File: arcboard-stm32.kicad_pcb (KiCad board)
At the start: 2 copper layers, 59.5 x 59.7 mm, 78 parts, among them J10 Conn_01x02_Socket, J5 Conn_01x02_Socket, J9 Conn_01x03_Socket, U1 XC6210B332MR-G, U10 1N4148W_C81598, U11 TS-1187A-B-A-B, U12 AO3401A, U13 AO3401A, U14 TS-1187A-B-A-B, U15 TS-1187A-B-A-B, U2 TYPE-C-31-M-13, U3 STM32F405RGTx, U4 PJ-320A, U5 BAV70S,115, U6 BAV70S,115, U7 BAV70S,115, U8 BAV70S,115, U9 BAV70S,115, Y1 Crystal_GND24

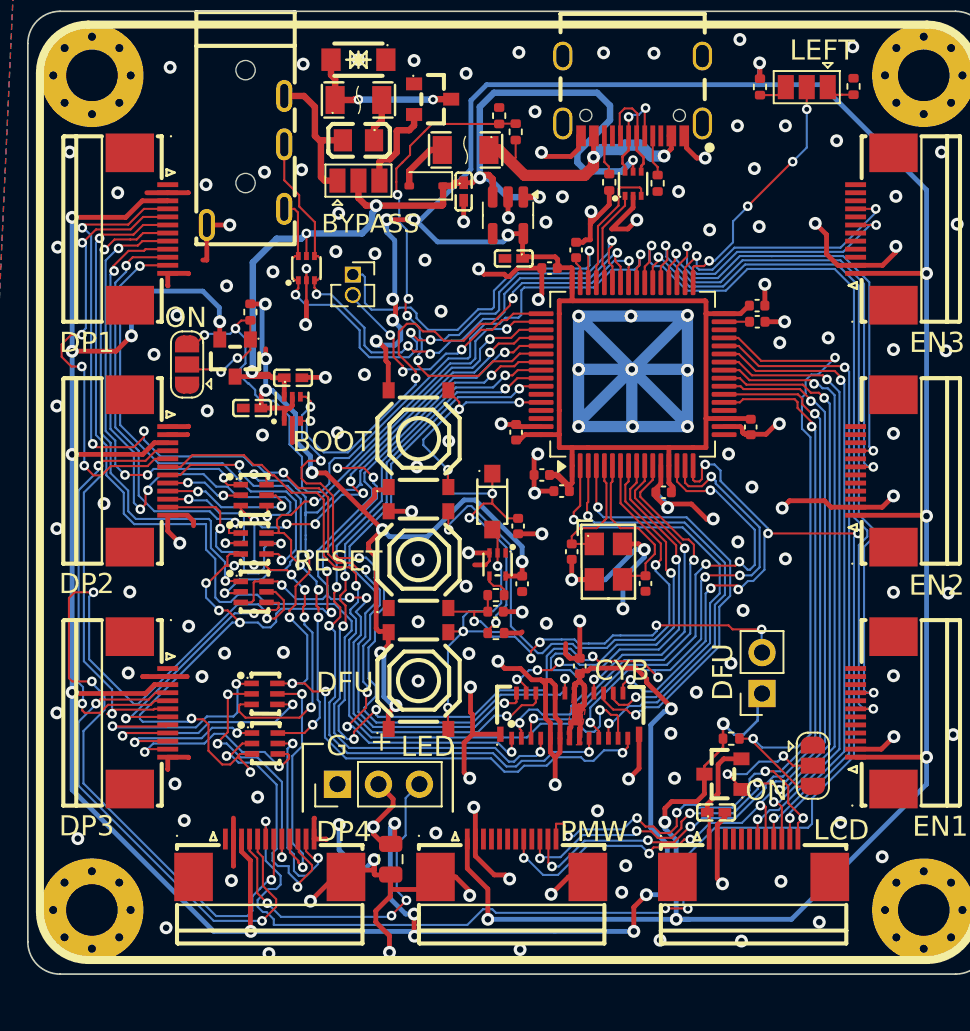
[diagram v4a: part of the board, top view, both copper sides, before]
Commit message: more trace pruning
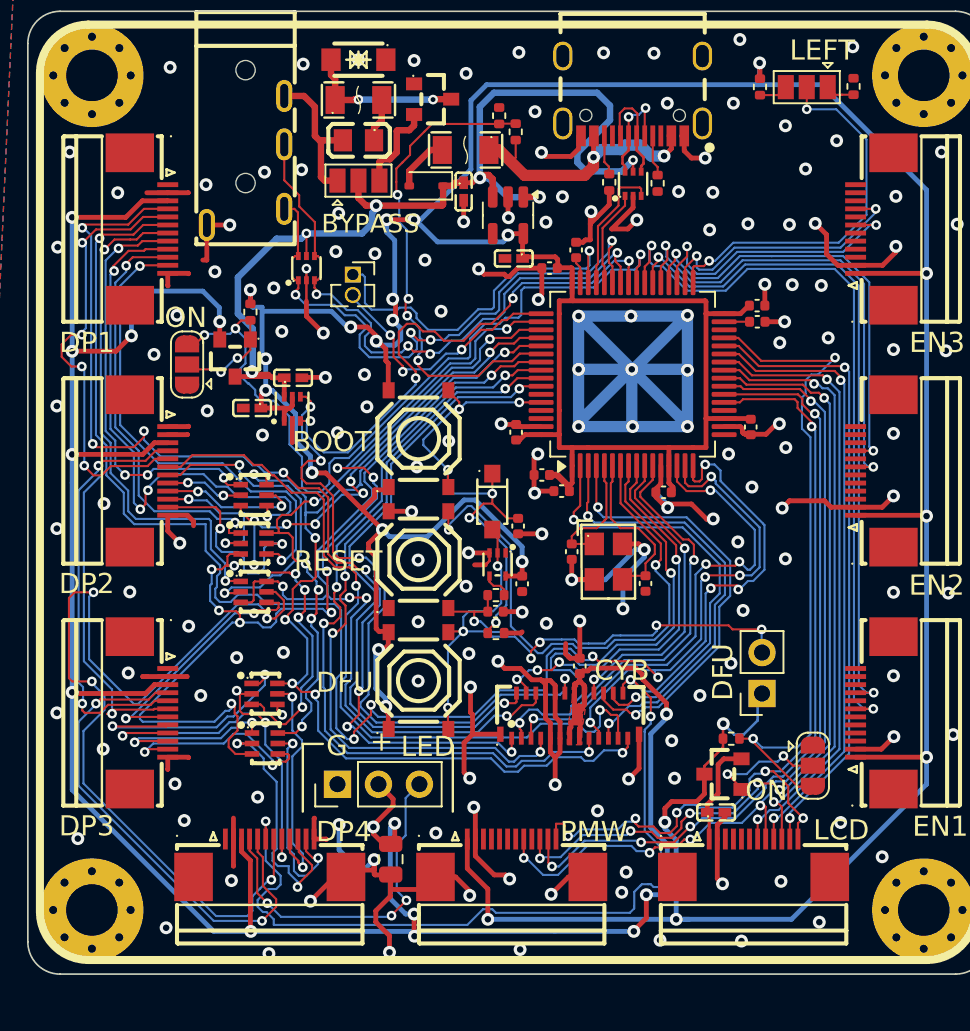
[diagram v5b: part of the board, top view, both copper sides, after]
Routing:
- net ROW6: track 98.6 -> 75.0 mm, vias 9 -> 6
- net +3V3: track 286.6 -> 295.1 mm, vias 22 -> 23
- net SPLIT_HAND: track 15.8 -> 23.7 mm, vias 4 -> 2
- net GND: track 240.9 -> 242.5 mm, vias 153 -> 162
- net Net-(J7-MOSI): track 14.4 -> 15.9 mm
- net Net-(J8-MOSI): track 15.6 -> 14.2 mm
- net COL8: track 46.9 -> 45.7 mm
- net Net-(J7-GP_AD2): track 15.2 -> 14.1 mm
- net Net-(J8-SPI_CS): track 17.1 -> 16.1 mm
- net +5V: track 63.9 -> 64.6 mm
- net SERIAL_TX: track 37.3 -> 38.0 mm
- net SERIAL_RX: track 36.8 -> 37.5 mm
- net Net-(J7-SPI_CS): track 9.89 -> 10.5 mm
- net COL10: track 63.7 -> 64.3 mm, vias 11 -> 10

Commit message: prepping for review
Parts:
- removed J10: Conn_01x02_Socket, Connector_PinSocket_1.27mm:PinSocket_1x02_P1.27mm_Vertical
- removed U12, U13: AO3401A, kicad-libraries:SOT-23_L2.9-W1.3-P1.90-LS2.4-BR
- added J2: Conn_01x04_Socket, Connector_PinSocket_1.00mm:PinSocket_1x04_P1.00mm_Vertical, F.Cu at (82.9, 82.9)
- added MOSFET2: AO3401A, kicad-libraries:SOT-23_L2.9-W1.3-P1.90-LS2.4-BR, F.Cu at (75.4, 84.0)
- added MOSFET3: AO3401A, kicad-libraries:SOT-23_L2.9-W1.3-P1.90-LS2.4-BR, F.Cu at (105.5, 109.8)
- C1: value 4.7uf -> 4.7uF
- C10, C20: value 4.7uf -> 4.7uF; footprint Capacitor_SMD:C_0402_1005Metric -> Capacitor_SMD:C_0805_2012Metric
- C11, C12, C14, C16, C17, C5, C7, C8, C9: value 100nf -> 100nF
- C13, C15, C27: value 1u -> 1uF; footprint kicad-libraries:C0402 -> Capacitor_SMD:C_0402_1005Metric
- C18, C19: value 100nf -> 100nF; footprint kicad-libraries:C0402 -> Capacitor_SMD:C_0402_1005Metric
- C2, C4: value 2.2uf -> 2.2uF
- J13, J14, J15, J16, J3, J4, J6, J7, J8: value ~ -> FFC05001-12SBA124W5M
- MOSFET1: value AO3401A_C347476 -> AO3401A
- R1: value 75k -> 51k
- moved R10 1.98 mm to (91.2, 68.8)
- moved R11 1.94 mm to (90.0, 68.0)
- moved C20 1.48 mm to (96.0, 101.8)
- moved C12 1.41 mm to (95.5, 93.7), turned to 90 degrees
- moved R4 0.96 mm to (101.8, 72.2)
- moved R5 0.89 mm to (98.4, 72.2)
- moved C10 0.55 mm to (94.0, 91.7)
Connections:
- J6 pad 10: Net-(J6-SPI_CS) -> COL9
- J6 pad 11: Net-(J6-MISO) -> COL10
- J6 pad 7: Net-(J6-GP_AD1) -> COL6
- J6 pad 8: Net-(J6-MOSI) -> COL7
- J6 pad 9: Net-(J6-GP_AD2) -> COL8
- R4 pad 1: SourceSinkPulldown -> CC1-SourceSinkPulldown
- R5 pad 1: SourceSinkPulldown -> CC2-SourceSinkPulldown
- U2 pad A5: SourceSinkPulldown -> CC1-SourceSinkPulldown
- U2 pad B5: SourceSinkPulldown -> CC2-SourceSinkPulldown
- U5 pad 1: Net-(J6-GP_AD1) -> COL6
- U6 pad 1: Net-(J6-MOSI) -> COL7
- U6 pad 4: Net-(J6-GP_AD2) -> COL8
- U7 pad 1: Net-(J6-SPI_CS) -> COL9
- U7 pad 4: Net-(J6-MISO) -> COL10
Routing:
- net Net-(J6-GP_AD2): track 34.1 -> 0.00 mm, vias 4 -> 0
- net COL8: track 45.7 -> 79.6 mm, vias 11 -> 15
- net Net-(J6-GP_AD1): track 31.9 -> 0.00 mm, vias 2 -> 0
- net COL6: track 54.3 -> 86.0 mm, vias 5 -> 7
- net Net-(J6-MISO): track 30.3 -> 0.00 mm, vias 2 -> 0
- net COL10: track 64.3 -> 94.1 mm, vias 10 -> 12
- net Net-(J6-SPI_CS): track 26.3 -> 0.00 mm, vias 2 -> 0
- net Net-(J6-MOSI): track 26.2 -> 0.00 mm, vias 4 -> 0
- net COL7: track 66.0 -> 91.9 mm, vias 7 -> 11
- net COL9: track 39.6 -> 65.3 mm, vias 6 -> 8
- net ROW4: track 74.5 -> 83.1 mm
- net +5V: track 64.6 -> 59.0 mm
- net SourceSinkPulldown: track 5.05 -> 0.00 mm
- net VBUS: track 17.5 -> 22.2 mm
- net ROW6: track 75.0 -> 78.9 mm
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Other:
- board text added: "EXT-DFU"
- board text added: "R L"
- board text added: "SWDIO SWCLK 3V3 GND"
- board text removed: "LEFT"

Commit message: before removal of usb port
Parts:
- removed C16: 100nF, Capacitor_SMD:C_0402_1005Metric
- removed REF1: SN74AHC1G14DRLR, kicad-libraries:SOT-553-5_L1.6-W1.2-P0.50-LS1.6-BL
- removed U14: TS-1187A-B-A-B, kicad-libraries:SW-SMD_4P-L5.1-W5.1-P3.70-LS6.5-TL_H1.5
- added C22: CL10A106MA8NRNC, Capacitor_SMD:C_0201_0603Metric, F.Cu at (87.5, 91.8)
- added J10: Conn_01x04_Socket, Connector_PinHeader_1.00mm:PinHeader_1x04_P1.00mm_Vertical, F.Cu at (110.0, 101.7)
- added R13: 0402WGF1002TCE, Resistor_SMD:R_0402_1005Metric, F.Cu at (88.3, 98.3)
- added R14: 0402WGF1000TCE, Resistor_SMD:R_0402_1005Metric, F.Cu at (88.8, 99.8)
- added R15: 0402WGF1001TCE, Resistor_SMD:R_0402_1005Metric, F.Cu at (89.8, 96.8)
- added R3: 0402WGF1002TCE, Resistor_SMD:R_0402_1005Metric, F.Cu at (89.8, 97.8)
- added R6: 0603WAF3303T5E, Resistor_SMD:R_0201_0603Metric, F.Cu at (88.3, 91.8)
- added R9: 0402WGF1003TCE, Resistor_SMD:R_0402_1005Metric, F.Cu at (87.2, 100.5)
- added U12: TYPE-C-31-M-13, kicad-libraries:USB-C_SMD-TYPE-C-31-M-12, F.Cu at (77.0, 67.8)
- added U13: 2N7002, kicad-libraries:SOT-23-3_L2.9-W1.3-P1.90-LS2.4-BR, F.Cu at (87.0, 94.3)
- R1: value 51k -> 0402WGF1004TCE
- R2: value 1k -> 0402WGF1002TCE
- U11: value TS-1187A-B-A-B -> W25Q16JVSSIQTR; footprint kicad-libraries:SW-SMD_4P-L5.1-W5.1-P3.70-LS6.5-TL_H1.5 -> kicad-libraries:SOIC-8_L5.3-W5.3-P1.27-LS8.0-BL
- U4: value PJ-320A -> 2N7002; footprint kicad-libraries:AUDIO-TH_XKB_PJ-320A -> kicad-libraries:SOT-23-3_L2.9-W1.3-P1.90-LS2.4-BR
- moved U11 28.2 mm to (109.0, 71.7), turned to 0 degrees
- moved U4 28.1 mm to (86.0, 98.0), turned to 90 degrees
- moved C14 23.7 mm to (109.6, 77.6), turned to 90 degrees
- moved R1 10.6 mm to (86.1, 92.0)
- moved R12 5.82 mm to (108.2, 65.4), turned to 90 degrees
- moved R2 4.03 mm to (88.3, 96.3), turned to -90 degrees
- moved R10 3.72 mm to (93.3, 65.7)
- moved R11 3.20 mm to (92.3, 65.7)
- moved C17 3.19 mm to (90.3, 99.4)
- moved F3 2.53 mm to (85.5, 68.0)
- moved JP3 2.50 mm to (112.1, 65.0)
- moved D4 2.40 mm to (85.4, 65.4)
- moved R20 2.23 mm to (109.2, 65.4)
- moved MOSFET1 2.20 mm to (89.8, 67.9)
- moved L1 2.10 mm to (85.1, 70.5)
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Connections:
- C14 pad 1: BOOT0 -> GND
- C14 pad 2: GND -> +3V3
- C17 pad 1: +3V3 -> GND
- C17 pad 2: GND -> NRST
- D5 pad 1: SERIAL_RX -> SERIAL_CONN_RX
- D5 pad 3: SERIAL_TX -> SERIAL_CONN_TX
- D5 pad 4: SERIAL_TX -> SERIAL_CONN_TX
- D5 pad 6: SERIAL_RX -> SERIAL_CONN_RX
- JP2 pad 1: /Serial_VBUS -> Serial_VBUS
- L1 pad 2: /Serial_VBUS -> Serial_VBUS
- R1 pad 1: GND -> BOOT0
- R1 pad 2: BOOT0 -> GND
- R2 pad 2: NRST -> Net-(U4-G)
- U10 pad 1: BOOT0 -> Net-(U10-K)
- U11 pad 1: +3V3 -> FLASH_CS
- U11 pad 2: +3V3 -> SPI1_MISO
- U11 pad 3: BOOT0 -> +3V3
- U11 pad 4: BOOT0 -> GND
- U3 pad 30: unconnected-(U3-PB11-Pad30) -> FLASH_CS
- U3 pad 42: SERIAL_TX -> SERIAL_CONN_TX
- U3 pad 43: SERIAL_RX -> SERIAL_CONN_RX
- U4 pad 2: /Serial_VBUS -> GND
- U4 pad 3: SERIAL_TX -> Net-(U4-D)
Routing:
- net BOOT0: track 31.6 -> 86.0 mm, vias 6 -> 9
- net SERIAL_CONN_RX: track 0.00 -> 41.8 mm, vias 0 -> 6
- net SERIAL_CONN_TX: track 0.00 -> 41.4 mm, vias 0 -> 6
- net SERIAL_TX: track 38.0 -> 0.00 mm, vias 4 -> 0
- net SERIAL_RX: track 35.7 -> 0.00 mm, vias 4 -> 0
- net SPI1_CLK: track 53.7 -> 85.4 mm, vias 6 -> 9
- net SPI1_MISO: track 48.6 -> 79.2 mm, vias 4 -> 7
- net SPI1_MOSI: track 54.2 -> 82.4 mm, vias 5 -> 8
- net FLASH_CS: track 0.00 -> 17.5 mm, vias 0 -> 4
- net Serial_VBUS: track 0.00 -> 14.4 mm
- net /Serial_VBUS: track 9.20 -> 0.00 mm
- net Net-(U13-D): track 1.81 -> 10.6 mm, vias 0 -> 2
- net VBUS_DETECT: track 28.4 -> 35.0 mm
- net Net-(JP3-A): track 1.80 -> 7.49 mm
- net Net-(U4-G): track 0.00 -> 5.64 mm, vias 0 -> 2
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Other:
- board text added: "DP1 = Dpad DP2-4 = Paddle EN1-2 = Top wheel encoders EN3 = Ring encoder CYB = Cyboard 25-pin LED = Gnd, +5v, WS2812 data ON = solder these for normal operation; else bypass EXT-DFU = activate DFU from external switch RESET = activate nRST from external switch BYPASS = solder arrow side to bypass R/L = handedness"
- board text removed: "+"
- board text removed: "G"
- board text removed: "RESET"

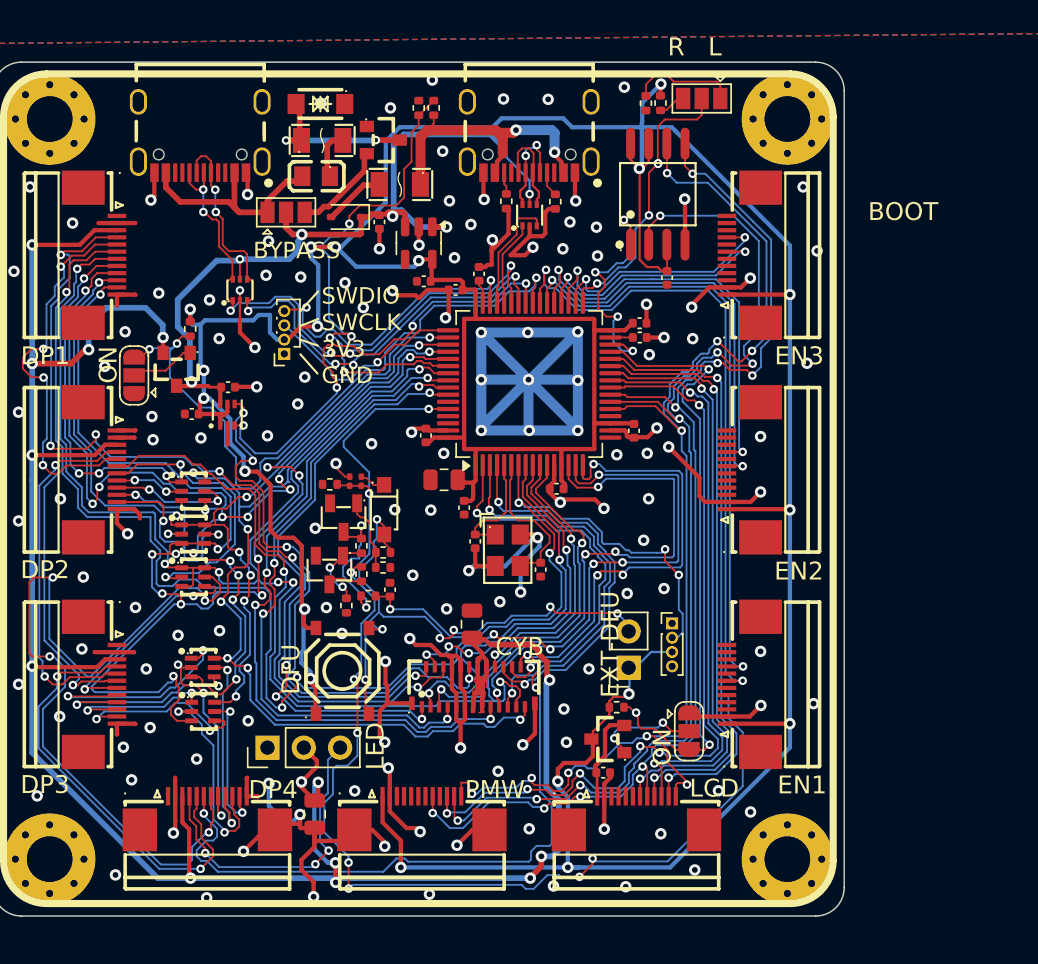
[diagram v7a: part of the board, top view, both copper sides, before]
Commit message: moving to separate split connector, adding flash
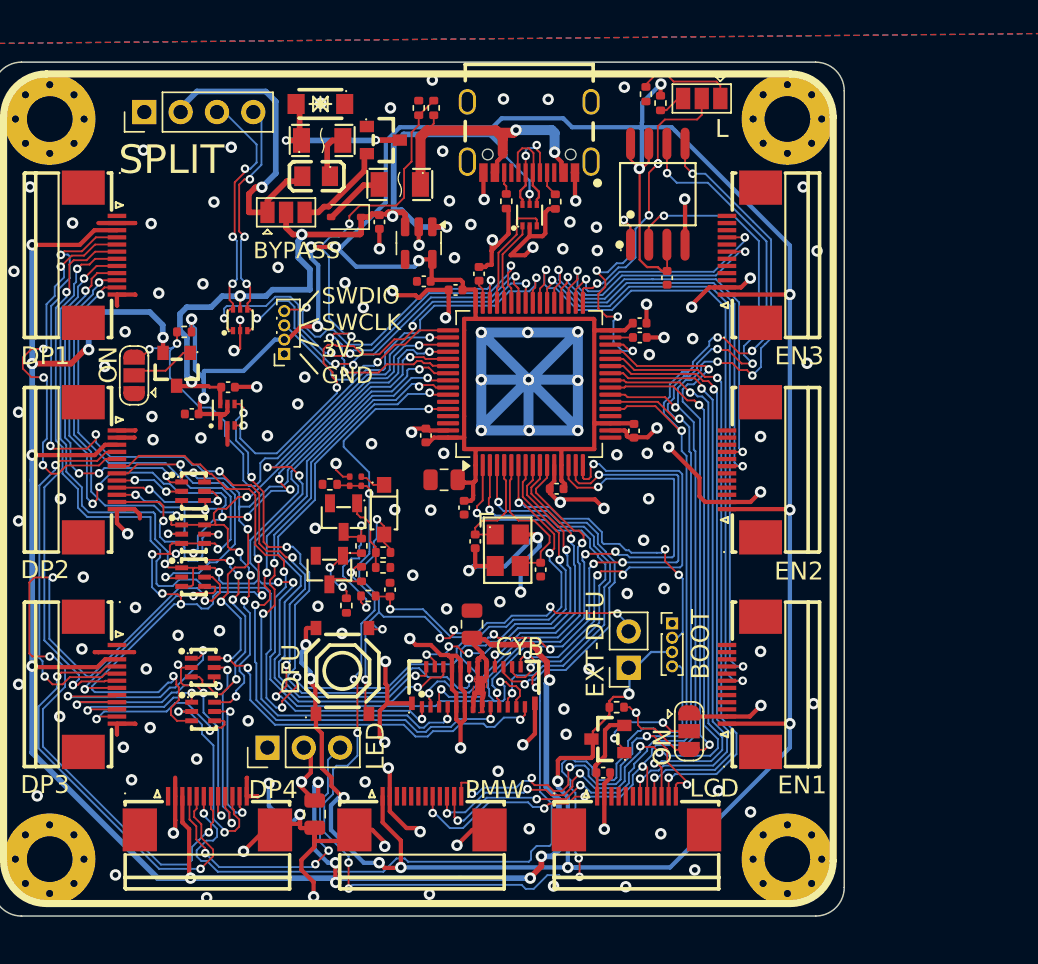
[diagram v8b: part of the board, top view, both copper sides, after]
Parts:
- removed U12: TYPE-C-31-M-13, kicad-libraries:USB-C_SMD-TYPE-C-31-M-12
- added J1: Conn_01x04_Socket, Connector_PinHeader_2.54mm:PinHeader_1x04_P2.54mm_Vertical, F.Cu at (73.1, 66.0)
- moved D5 2.10 mm to (79.8, 80.5)
- moved R12 0.63 mm to (108.2, 64.7)
- moved R7 0.47 mm to (75.9, 81.4), turned to 180 degrees
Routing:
- net Serial_VBUS: track 14.4 -> 21.8 mm, vias 0 -> 1
- net +3V3: track 297.6 -> 290.5 mm
- net SERIAL_CONN_RX: track 41.8 -> 48.5 mm, vias 6 -> 7
- net GND: track 237.2 -> 231.7 mm, vias 143 -> 142
- net BOOT0: track 86.0 -> 90.6 mm
- net SERIAL_CONN_TX: track 41.4 -> 44.0 mm, vias 6 -> 7
- net SPI1_CLK: track 85.4 -> 87.6 mm
- net LED_KEYS_DI: track 41.4 -> 39.4 mm
- net +5V: track 59.3 -> 60.8 mm
- net RGB_ON: track 48.1 -> 47.2 mm
- net Net-(JP3-A): track 7.49 -> 6.86 mm
- net RGB_5V: track 162.5 -> 161.9 mm
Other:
- board text added: "L"
- board text added: "SPLIT"
- board text added: "TX RX 5V GND"
- board text removed: "R L"
